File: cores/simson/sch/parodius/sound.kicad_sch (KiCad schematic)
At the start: 15 parts

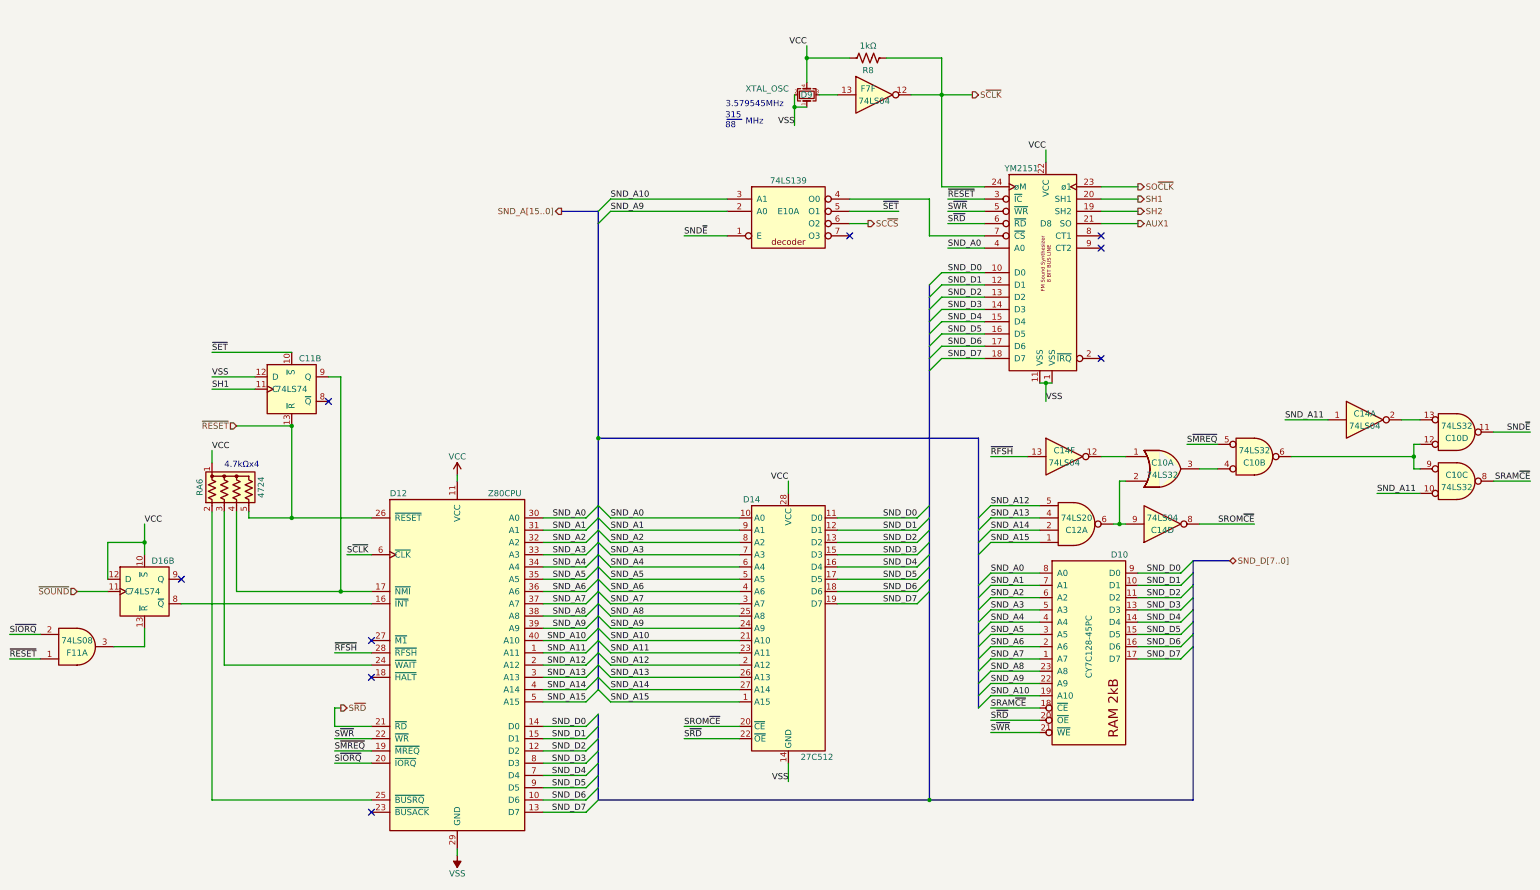
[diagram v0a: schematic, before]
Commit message: simson: Parodius da! boots up
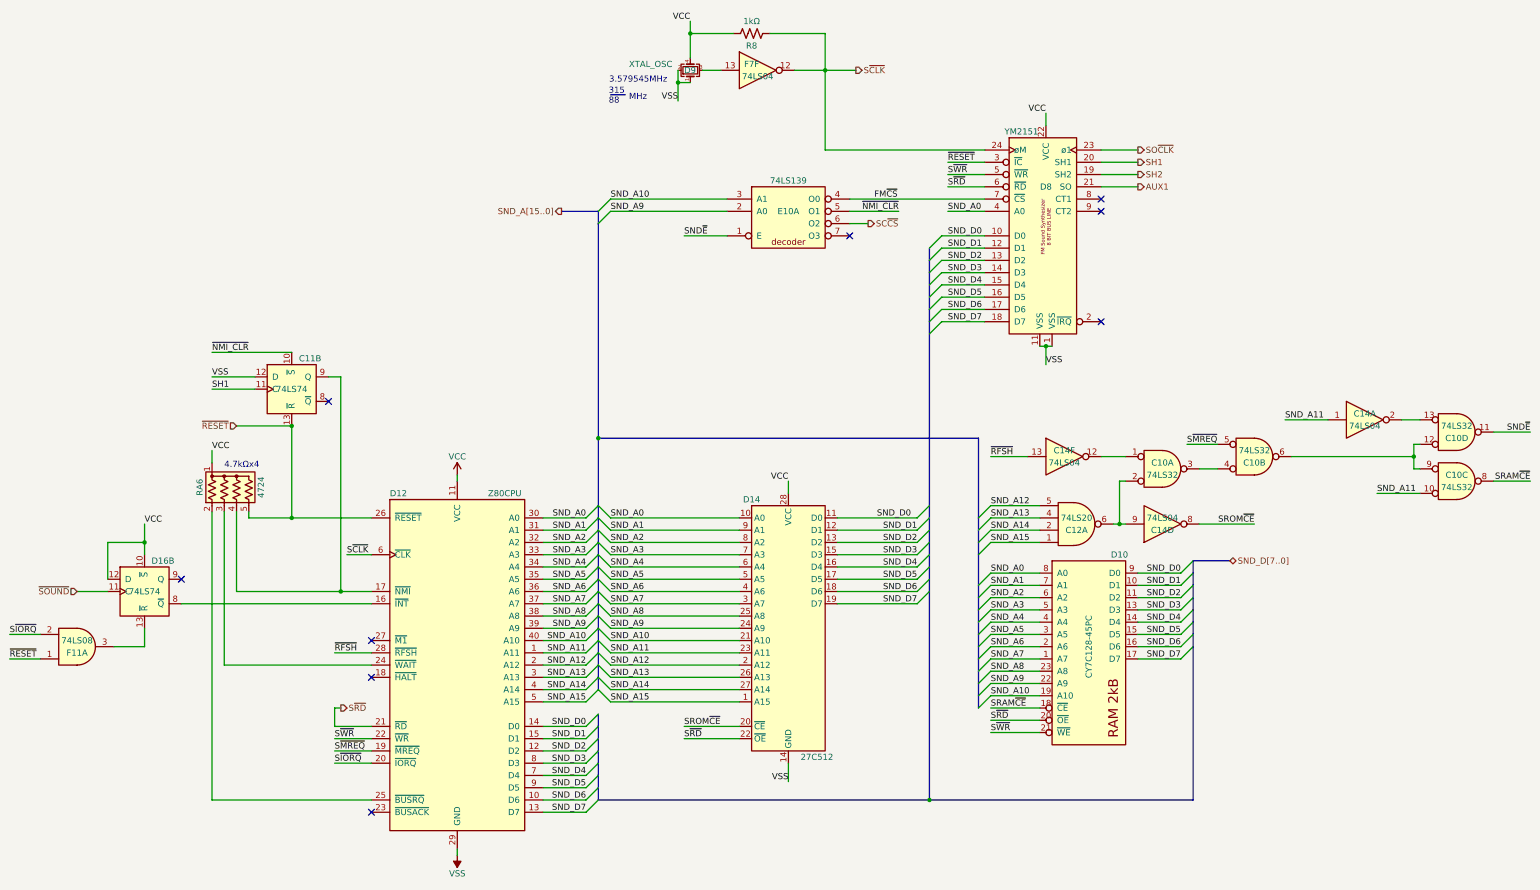
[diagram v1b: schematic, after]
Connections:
- net FM~{CS}: now reaches D8.7 (~{CS}), E10.4 (O0)
- net ~{SET} renamed ~{NMI_CLR}
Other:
- moved on the sheet: D8, D9, F7F, R8

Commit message: wip #517 paroda
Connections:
- net FM~{CS}: no longer names the net of D8.7 (~{CS}), E10.4 (O0)
- net ~{NMI_CLR} renamed ~{SET}
- net ~{SOUND} renamed ~{SOON}
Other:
- moved on the sheet: D8, D9, F7F, R8

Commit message: issue #517 done
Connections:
- net ~{RESET} renamed ~{WDOGRST}
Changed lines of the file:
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@@
     (effects (font (size 1.27 1.27)) (justify left bottom))
   )
-  (label "~{RESET}" (at 242.57 85.09 0) (fields_autoplaced)
+  (label "~{WDOGRST}" (at 242.57 85.09 0) (fields_autoplaced)
     (effects (font (size 1.27 1.27)) (justify left bottom))
   )
@@
     (effects (font (size 1.27 1.27)) (justify left bottom))
   )
-  (label "~{RESET}" (at 48.26 180.34 0) (fields_autoplaced)
+  (label "~{WDOGRST}" (at 48.26 180.34 0) (fields_autoplaced)
     (effects (font (size 1.27 1.27)) (justify left bottom))
   )
@@
     (effects (font (size 1.27 1.27)) (justify left))
   )
-  (hierarchical_label "~{RESET}" (shape input) (at 95.25 132.08 180) (fields_autoplaced)
+  (hierarchical_label "~{WDOGRST}" (shape input) (at 95.25 132.08 180) (fields_autoplaced)
     (effects (font (size 1.27 1.27)) (justify right))
   )

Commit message: sch: changed copyright notice
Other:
- company: Esperanza Triana -> JOTEGO
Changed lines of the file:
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@@
     (date "2023-05-09")
     (rev "José Tejada G.")
-    (company "Esperanza Triana")
+    (company "JOTEGO")
     (comment 1 "www.patreon.com/jotego")
     (comment 2 "JOTEGO")
